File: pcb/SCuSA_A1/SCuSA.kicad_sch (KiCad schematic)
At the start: 75 parts, among them J101 USB4135-GF-A, J102 JST_S2B-PH-K-x, J103 Binding_Post_PKI_10_A_Au, J104 Binding_Post_PKI_10_A_Au, J105 SMA_Straight_Jack_Female, J107 77311-118-02LF, J108 77311-118-02LF, Q101 DMN2041LSD, SW101 JS202011CQN, SW102 JS202011CQN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

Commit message: Minor SCH and PCB modifications
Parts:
- added C121: C, Capacitor_SMD:C_0603_1608Metric_Pad1.08x0.95mm_HandSolder, symbol Device:C_Small
- added R121: R, Resistor_SMD:R_0603_1608Metric_Pad0.98x0.95mm_HandSolder, symbol Device:R
- U105: value AD8410AWBRZ -> AD8418AWBRZ; symbol Amplifier_Current:AD8418 -> Amplifier_Current_User:AD8418AWBRZ; MPN (none) -> AD8418AWBRZ; Manufacturer (none) -> Analog Devices; SPN 505-AD8410AWBRZ-ND -> 505-AD8418AWBRZ-ND
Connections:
- net GND: now also C121.2
- net at R118.1, U106.2 (-), U106.6: now also R121.1
- new net: C121.1, R121.2
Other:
- note added: "AD8210A for 2.2 MHz BW AD8418A for 250 kHz BW"
- note added: "Connect for battery pack with built in protection. In this case do not populate battery protection components."
- note added: "Optional snubber"
- note added: "Scaling I = 20 * R_{sense} * V_{out} With R_{sense} = 50 mΩ a current of +3 A results an output voltage of +3 V. Negative output swing is limited to -Vx."
- note removed: "AD8210 for 450 kHz BW AD8418AWBRZ for 250kHz BW"
- note removed: "For battery pack with integrated protection."
- note removed: "Scaling I = 20 * R_{sense} * V_{out} With R_{sense} = 50 mΩ a current of +3 A results an output voltage of +3 V."
- company: (none) -> fl0m0
- title: (none) -> SCuSA - Scope Current Sense Amplifier
- moved on the sheet: C117, SW102B

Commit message: RevA1
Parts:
- added R122: 0R,0603, Resistor_SMD:R_0603_1608Metric_Pad0.98x0.95mm_HandSolder, symbol Resistor_User:0R,0603
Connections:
- net GND: now also R122.2
- net at J101.M (SHIELD): now also R122.1
- no-connect marks 5 -> 4
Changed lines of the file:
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@@
   (junction (at 66.04 27.94) (diameter 0) (color 0 0 0 0)
   )
-  (no_connect (at 46.99 49.53))
   (no_connect (at 143.51 31.75))
   (no_connect (at 252.73 121.92))
@@
     (stroke (width 0) (type default))
   )
-  (wire (pts (xy 52.07 45.72) (xy 52.07 50.8))
+  (wire (pts (xy 52.07 45.72) (xy 52.07 46.99))
     (stroke (width 0) (type default))
   )
@@
     (stroke (width 0) (type default))
   )
+  (wire (pts (xy 46.99 53.34) (xy 46.99 49.53))
+    (stroke (width 0) (type default))
+  )
   (wire (pts (xy 213.36 114.3) (xy 213.36 111.76))
     (stroke (width 0) (type default))
@@
     )
   )
+  (symbol (lib_id "Resistor_User:0R,0603") (at 46.99 57.15 0) (unit 1)
+    (in_bom yes) (on_board yes) (dnp no) (fields_autoplaced)
+    (property "Reference" "R122" (at 49.53 55.88 0)
+      (effects (font (size 1.27 1.27)) (justify left))
+    )
+    (property "Value" "0R,0603" (at 48.895 54.61 0)
+      (effects (font (size 1.27 1.27)) (justify left) hide)
+    )
+    (property "Footprint" "Resistor_SMD:R_0603_1608Metric_Pad0.98x0.95mm_HandSolder" (at 49.53 67.31 0)
+      (effects (font (size 1.27 1.27)) hide)
+    )
+    (property "Datasheet" "~" (at 49.53 61.595 0)
+      (effects (font (size 1.27 1.27)) hide)
+    )
+    (property "Resistance" "0R" (at 49.53 58.42 0)
+      (effects (font (size 1.27 1.27)) (justify left))
+    )
+    (property "Tolerance" "1%" (at 52.07 57.15 0)
+      (effects (font (size 1.27 1.27)) (justify left) hide)
+    )
+    (property "Power" "0.1W" (at 57.785 57.15 0)
+      (effects (font (size 1.27 1.27)) hide)
+    )
+    (property "Package" "0603" (at 51.435 59.69 0)
+      (effects (font (size 1.27 1.27)) hide)
+    )
+    (pin "1")
+    (pin "2")
+    (instances
+      (project "SCuSA"
+        (path "/7c524ebf-103a-4dc7-9ca9-e5a941b364b9"
+          (reference "R122") (unit 1)
+        )
+      )
+    )
+  )
   (symbol (lib_id "Battery_Management:BQ297xy") (at 214.63 40.64 0) (mirror y) (unit 1)
     (in_bom yes) (on_board yes) (dnp no) (fields_autoplaced)
@@
     )
   )
-  (symbol (lib_id "power:GND") (at 52.07 50.8 0) (mirror y) (unit 1)
+  (symbol (lib_id "power:GND") (at 52.07 46.99 0) (mirror y) (unit 1)
     (in_bom yes) (on_board yes) (dnp no) (fields_autoplaced)
-    (property "Reference" "#PWR0109" (at 52.07 57.15 0)
+    (property "Reference" "#PWR0109" (at 52.07 53.34 0)
       (effects (font (size 1.27 1.27)) hide)
     )
-    (property "Value" "GND" (at 52.07 55.88 0)
+    (property "Value" "GND" (at 52.07 52.07 0)
       (effects (font (size 1.27 1.27)))
     )
-    (property "Footprint" "" (at 52.07 50.8 0)
+    (property "Footprint" "" (at 52.07 46.99 0)
       (effects (font (size 1.27 1.27)) hide)
     )
-    (property "Datasheet" "" (at 52.07 50.8 0)
+    (property "Datasheet" "" (at 52.07 46.99 0)
       (effects (font (size 1.27 1.27)) hide)
     )
@@
         )
       )
+    )
+  )
+  (symbol (lib_id "power:GND") (at 46.99 60.96 0) (mirror y) (unit 1)
+    (in_bom yes) (on_board yes) (dnp no) (fields_autoplaced)
+    (property "Reference" "#PWR0116" (at 46.99 67.31 0)
+      (effects (font (size 1.27 1.27)) hide)
+    )
+    (property "Value" "GND" (at 46.99 66.04 0)
+      (effects (font (size 1.27 1.27)))
+    )
+    (property "Footprint" "" (at 46.99 60.96 0)
+      (effects (font (size 1.27 1.27)) hide)
+    )
+    (property "Datasheet" "" (at 46.99 60.96 0)
+      (effects (font (size 1.27 1.27)) hide)
+    )
+    (pin "1")
+    (instances
+      (project "SCuSA"
+        (path "/7c524ebf-103a-4dc7-9ca9-e5a941b364b9"
+          (reference "#PWR0116") (unit 1)
+        )
+      )

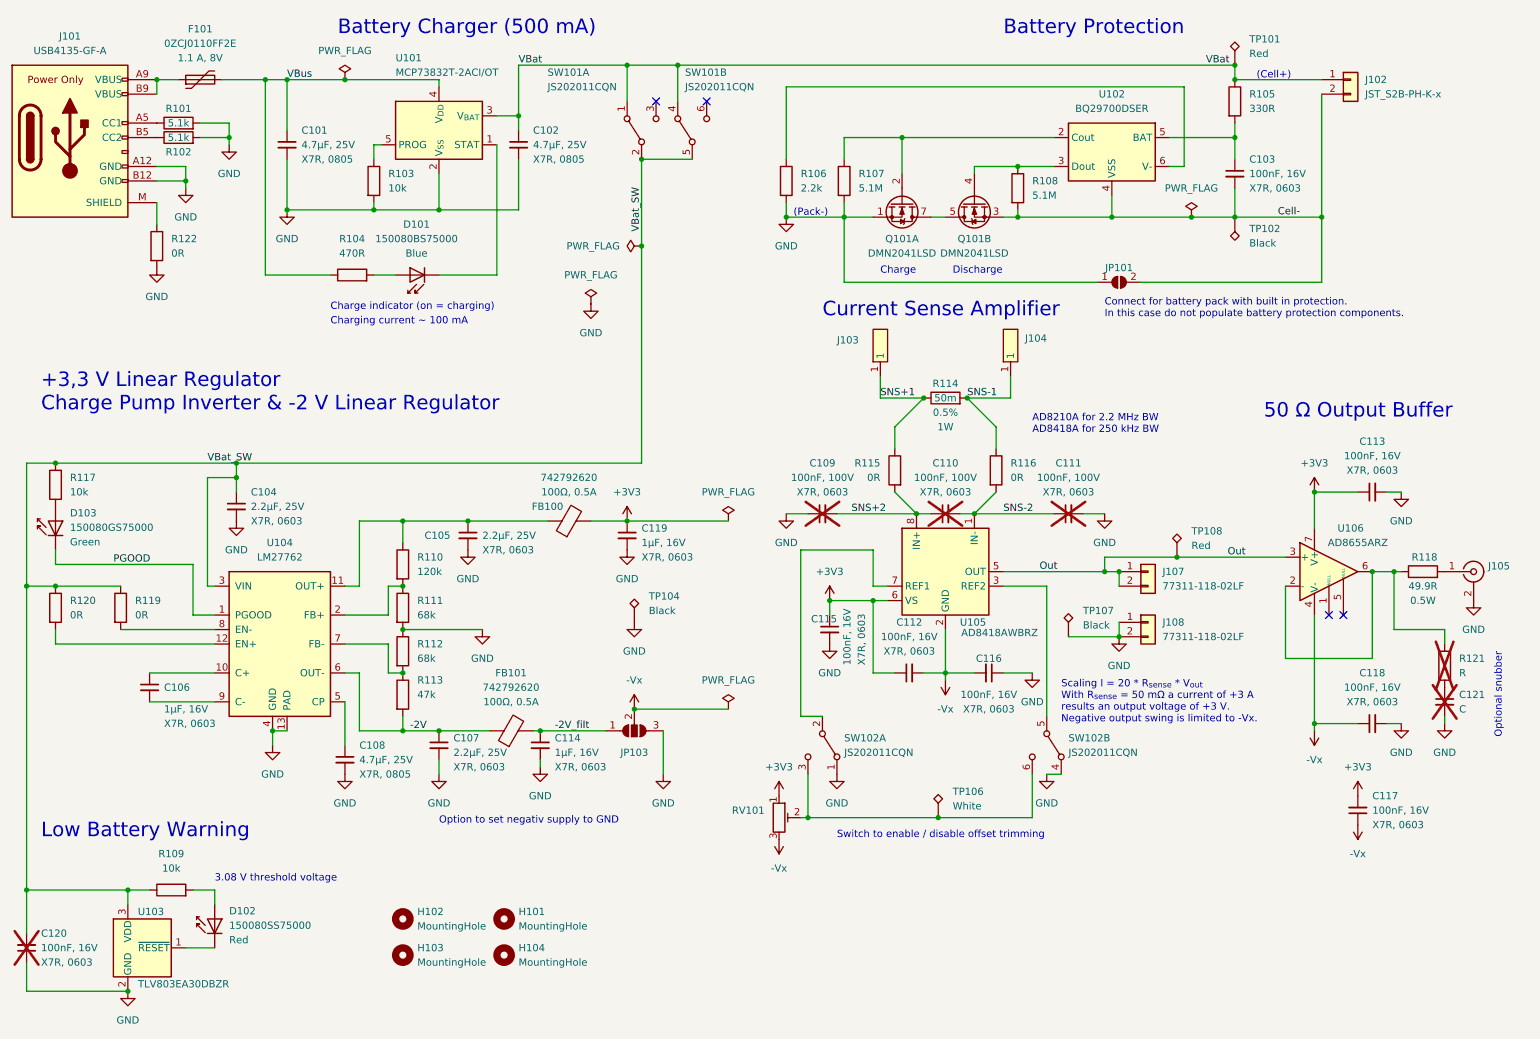
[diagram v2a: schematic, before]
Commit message: Increase charge current, change LED resistors
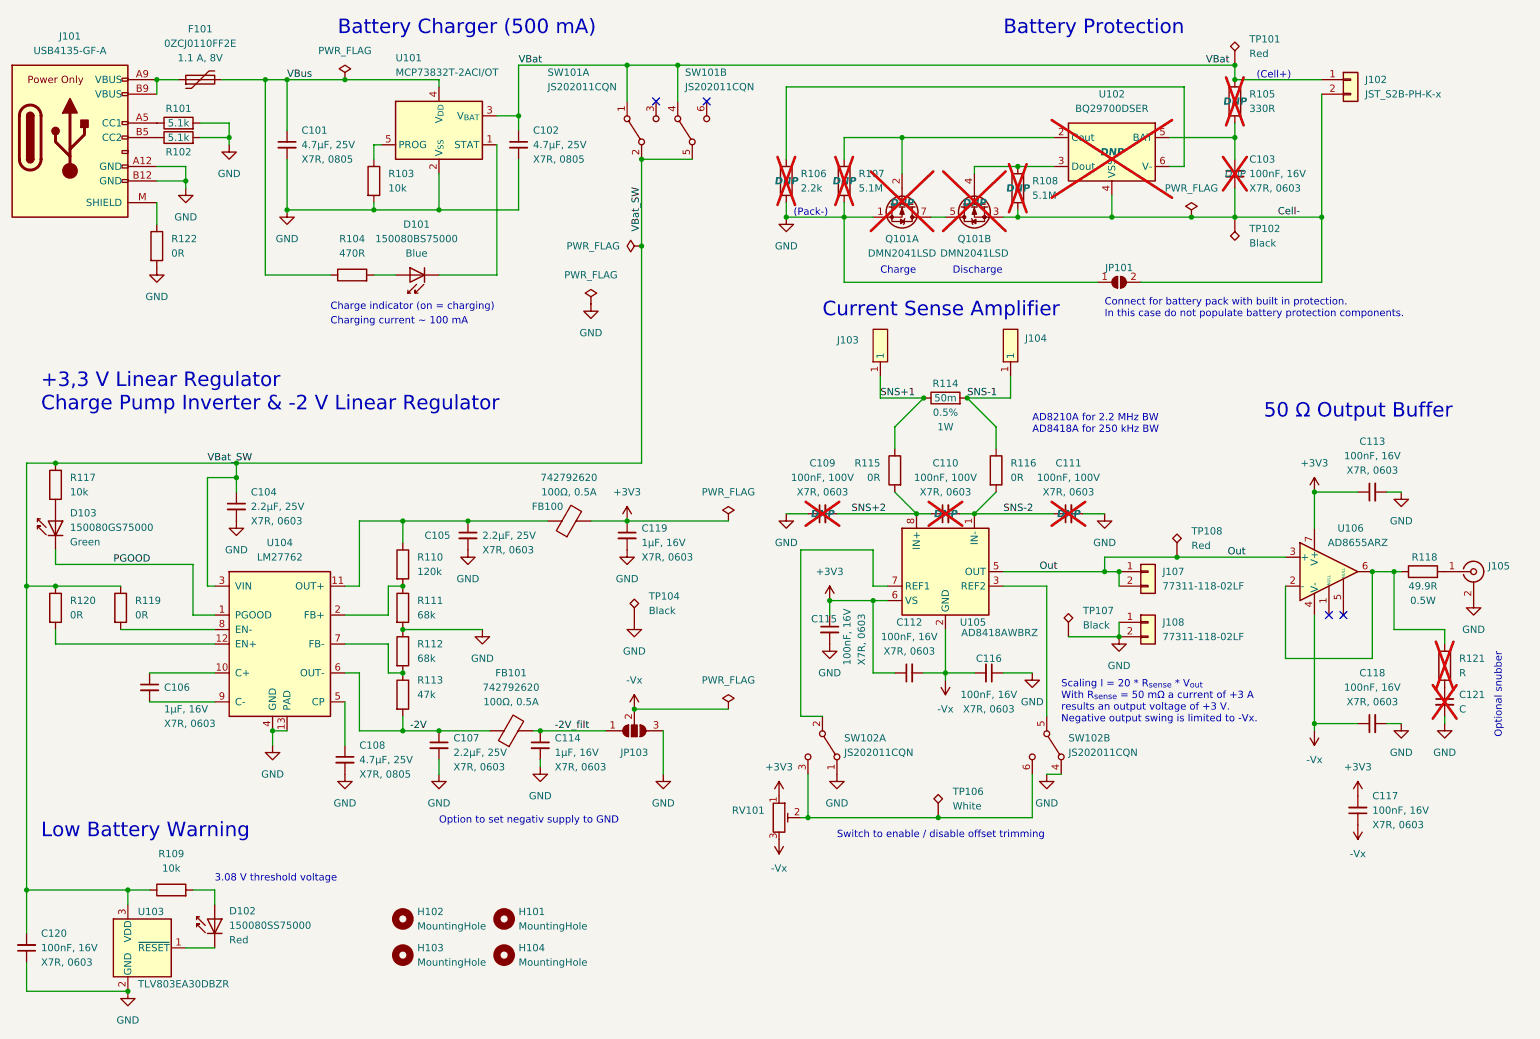
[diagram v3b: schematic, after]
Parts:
- C101, C102: value 1uF,16V,X7R,0603 -> 4.7uF,25V,X7R,0805
- C103, Q101, R105, R106, R107, R108, U102: DNP (none) -> DNP; now not fitted
- C109, C110, C111: DNP (none) -> DNP
- C120: now fitted
- FB100, FB101: footprint Inductor_SMD:L_1206_3216Metric_Pad1.42x1.75mm_HandSolder -> Inductor_SMD:L_0603_1608Metric_Pad1.05x0.95mm_HandSolder
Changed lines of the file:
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@@
   )
   (symbol (lib_id "Capacitor_User:100nF,16V,X7R,0603") (at 24.13 180.34 180) (unit 1)
-    (in_bom yes) (on_board yes) (dnp yes) (fields_autoplaced)
+    (in_bom yes) (on_board yes) (dnp no) (fields_autoplaced)
     (property "Reference" "C120" (at 26.67 177.7936 0)
       (effects (font (size 1.27 1.27)) (justify right))
@@
   )
   (symbol (lib_id "Resistor_User:2.2k,0603") (at 157.48 45.72 0) (unit 1)
-    (in_bom yes) (on_board yes) (dnp no)
+    (in_bom yes) (on_board yes) (dnp yes)
     (property "Reference" "R106" (at 160.02 44.45 0)
       (effects (font (size 1.27 1.27)) (justify left))
@@
       (effects (font (size 1.27 1.27)) hide)
     )
+    (property "DNP" "DNP" (at 157.48 45.72 0)
+      (effects (font (size 1.27 1.27) bold italic))
+    )
     (pin "1")
     (pin "2")
@@
       (effects (font (size 1.27 1.27)) (justify left))
     )
-    (property "Value" "1uF,16V,X7R,0603" (at 73.66 45.72 0)
+    (property "Value" "4.7uF,25V,X7R,0805" (at 72.39 43.18 0)
       (effects (font (size 1.27 1.27)) (justify left) hide)
     )
@@
   )
   (symbol (lib_id "Battery_Management:BQ297xy") (at 214.63 40.64 0) (mirror y) (unit 1)
-    (in_bom yes) (on_board yes) (dnp no) (fields_autoplaced)
+    (in_bom yes) (on_board yes) (dnp yes) (fields_autoplaced)
     (property "Reference" "U102" (at 214.63 30.48 0)
       (effects (font (size 1.27 1.27)))
@@
       (effects (font (size 1.27 1.27)) hide)
     )
+    (property "DNP" "DNP" (at 214.63 40.64 0)
+      (effects (font (size 1.27 1.27) bold italic))
+    )
     (pin "1")
     (pin "2")
@@
       (effects (font (size 1.27 1.27)))
     )
+    (property "DNP" "DNP" (at 163.83 104.14 90)
+      (effects (font (size 1.27 1.27) bold italic))
+    )
     (pin "1")
     (pin "2")
@@
       (effects (font (size 1.27 1.27)))
     )
+    (property "DNP" "DNP" (at 207.01 104.14 90)
+      (effects (font (size 1.27 1.27) bold italic))
+    )
     (pin "1")
     (pin "2")
@@
   )
   (symbol (lib_id "Resistor_User:330R,0603") (at 236.22 31.75 0) (unit 1)
-    (in_bom yes) (on_board yes) (dnp no)
+    (in_bom yes) (on_board yes) (dnp yes)
     (property "Reference" "R105" (at 238.76 30.48 0)
       (effects (font (size 1.27 1.27)) (justify left))
@@
       (effects (font (size 1.27 1.27)) hide)
     )
+    (property "DNP" "DNP" (at 236.22 31.75 0)
+      (effects (font (size 1.27 1.27) bold italic))
+    )
     (pin "1")
     (pin "2")
@@
   )
   (symbol (lib_id "Resistor_User:5.1M,0603") (at 198.12 46.99 0) (unit 1)
-    (in_bom yes) (on_board yes) (dnp no) (fields_autoplaced)
+    (in_bom yes) (on_board yes) (dnp yes) (fields_autoplaced)
     (property "Reference" "R108" (at 200.66 45.72 0)
       (effects (font (size 1.27 1.27)) (justify left))
@@
       (effects (font (size 1.27 1.27)) hide)
     )
+    (property "DNP" "DNP" (at 198.12 46.99 0)
+      (effects (font (size 1.27 1.27) bold italic))
+    )
     (pin "1")
     (pin "2")
@@
     )
   )
-  (symbol (lib_id "Ferrite_User:742792620") (at 119.38 105.41 90) (unit 1)
+  (symbol (lib_name "742792620_1") (lib_id "Ferrite_User:742792620") (at 119.38 105.41 90) (unit 1)
     (in_bom yes) (on_board yes) (dnp no)
     (property "Reference" "FB100" (at 115.57 102.87 90)
@@
       (effects (font (size 1.27 1.27)))
     )
-    (property "Footprint" "Inductor_SMD:L_1206_3216Metric_Pad1.42x1.75mm_HandSolder" (at 119.38 107.188 90)
+    (property "Footprint" "Inductor_SMD:L_0603_1608Metric_Pad1.05x0.95mm_HandSolder" (at 119.38 107.188 90)
       (effects (font (size 1.27 1.27)) hide)
     )
@@
   )
   (symbol (lib_id "Transistor_FET_User:DMN2041LSD") (at 190.5 49.53 90) (mirror x) (unit 2)
-    (in_bom yes) (on_board yes) (dnp no)
+    (in_bom yes) (on_board yes) (dnp yes)
     (property "Reference" "Q101" (at 190.5 55.88 90)
       (effects (font (size 1.27 1.27)))
@@
       (effects (font (size 1.27 1.27)) hide)
     )
+    (property "DNP" "DNP" (at 190.5 49.53 90)
+      (effects (font (size 1.27 1.27) bold italic))
+    )
     (pin "1")
     (pin "2")
@@
   )
   (symbol (lib_id "Transistor_FET_User:DMN2041LSD") (at 177.8 49.53 270) (unit 1)
-    (in_bom yes) (on_board yes) (dnp no)
+    (in_bom yes) (on_board yes) (dnp yes)
     (property "Reference" "Q101" (at 177.8 55.88 90)
       (effects (font (size 1.27 1.27)))
@@
       (effects (font (size 1.27 1.27)) hide)
     )
+    (property "DNP" "DNP" (at 177.8 49.53 90)
+      (effects (font (size 1.27 1.27) bold italic))
+    )
     (pin "1")
     (pin "2")
@@
       (effects (font (size 1.27 1.27)))
     )
-    (property "Footprint" "Inductor_SMD:L_1206_3216Metric_Pad1.42x1.75mm_HandSolder" (at 109.22 144.018 90)
+    (property "Footprint" "Inductor_SMD:L_0603_1608Metric_Pad1.05x0.95mm_HandSolder" (at 109.22 144.018 90)
       (effects (font (size 1.27 1.27)) hide)
     )
@@
       (effects (font (size 1.27 1.27)))
     )
+    (property "DNP" "DNP" (at 185.42 104.14 90)
+      (effects (font (size 1.27 1.27) bold italic))
+    )
     (pin "1")
     (pin "2")
@@
   )
   (symbol (lib_id "Capacitor_User:100nF,16V,X7R,0603") (at 236.22 44.45 0) (unit 1)
-    (in_bom yes) (on_board yes) (dnp no)
+    (in_bom yes) (on_board yes) (dnp yes)
     (property "Reference" "C103" (at 238.76 41.9163 0)
       (effects (font (size 1.27 1.27)) (justify left))
@@
       (effects (font (size 1.27 1.27)) (justify left))
     )
+    (property "DNP" "DNP" (at 236.22 44.45 0)
+      (effects (font (size 1.27 1.27) italic))
+    )
     (pin "1")
     (pin "2")
@@
   )
   (symbol (lib_id "Resistor_User:5.1M,0603") (at 167.64 45.72 0) (unit 1)
-    (in_bom yes) (on_board yes) (dnp no) (fields_autoplaced)
+    (in_bom yes) (on_board yes) (dnp yes) (fields_autoplaced)
     (property "Reference" "R107" (at 170.18 44.45 0)
       (effects (font (size 1.27 1.27)) (justify left))
@@
       (effects (font (size 1.27 1.27)) hide)
     )
+    (property "DNP" "DNP" (at 167.64 45.72 0)
+      (effects (font (size 1.27 1.27) bold italic))
+    )
     (pin "1")
     (pin "2")
@@
       (effects (font (size 1.27 1.27)) (justify left))
     )
-    (property "Value" "1uF,16V,X7R,0603" (at 114.3 45.72 0)
+    (property "Value" "4.7uF,25V,X7R,0805" (at 114.3 45.72 0)
       (effects (font (size 1.27 1.27)) (justify left) hide)
     )
